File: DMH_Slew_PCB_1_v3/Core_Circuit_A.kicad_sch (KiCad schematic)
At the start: 0 parts

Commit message: V3 sch redesign ongoing
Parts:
- added C10, C11, C3, C4: 100nF, Capacitor_THT:C_Disc_D4.3mm_W1.9mm_P5.00mm, symbol Device:C
- added C14: 22nF, Capacitor_THT:C_Disc_D4.3mm_W1.9mm_P5.00mm, symbol Device:C
- added C15: 220nF, Capacitor_THT:C_Disc_D4.3mm_W1.9mm_P5.00mm, symbol Device:C
- added C6, C7, C8: 10pF, Capacitor_THT:C_Disc_D3.0mm_W2.0mm_P2.50mm, symbol Device:C
- added C9: 2.2nF, Capacitor_THT:C_Disc_D4.3mm_W1.9mm_P5.00mm, symbol Device:C
- added J1, J2, J3: TS_Jack_6.35mm_Sw, SynthStuff:CUI_MJ-63052A, symbol SynthStuff:TS_Jack_6.35mm_Sw
- added J11, J13: Conn_02x03_Top_Bottom, Connector_PinHeader_2.54mm:PinHeader_2x03_P2.54mm_Horizontal, symbol Connector_Generic:Conn_02x03_Top_Bottom
- added J12, J14: Conn_02x06_Top_Bottom, Connector_PinHeader_2.54mm:PinHeader_2x06_P2.54mm_Horizontal, symbol Connector_Generic:Conn_02x06_Top_Bottom
- added J15, J16: Conn_01x08, Connector_PinHeader_2.54mm:PinHeader_1x08_P2.54mm_Vertical, symbol Connector_Generic:Conn_01x08
- added Q1, Q2: BC548, Package_TO_SOT_THT:TO-92L_Inline_Wide, symbol Transistor_BJT:BC548
- added Q3, Q4: BC558, Package_TO_SOT_THT:TO-92L_Inline_Wide, symbol Transistor_BJT:BC558
- added R1, R14, R26: 1k, Resistor_THT:R_Axial_DIN0207_L6.3mm_D2.5mm_P7.62mm_Horizontal, symbol Device:R_US
- added R10, R11, R12, R13, R16, R2, R22, R23, R5, R6, R7, R8, R9: 100k, Resistor_THT:R_Axial_DIN0207_L6.3mm_D2.5mm_P7.62mm_Horizontal, symbol Device:R_US
- added R15, R24, R25: 220k, Resistor_THT:R_Axial_DIN0207_L6.3mm_D2.5mm_P7.62mm_Horizontal, symbol Device:R_US
- added R17: 10k, Resistor_THT:R_Axial_DIN0207_L6.3mm_D2.5mm_P7.62mm_Horizontal, symbol Device:R_US
- added R18, R19, R20, R21: 1k8, Resistor_THT:R_Axial_DIN0207_L6.3mm_D2.5mm_P7.62mm_Horizontal, symbol Device:R_US
- added R3, R4: 56k, Resistor_THT:R_Axial_DIN0207_L6.3mm_D2.5mm_P7.62mm_Horizontal, symbol Device:R_US
- added RV1, RV2: 100k, SynthStuff:Potentiometer_Alpha_RD901F-40-00D_Single_Vertical, symbol Device:R_Potentiometer_US
- added SW1: SW_DPDT_3way, SynthStuff:Toggle_Switch_2_Poles_TE, symbol SynthStuff:Switch_DPDT
- added SW2: SW_DPDT, SynthStuff:Toggle_Switch_2_Poles_TE, symbol SynthStuff:Switch_DPDT
- added SW3: SPDT_OnOffOn, SynthStuff:Toggle_Switch_TE, symbol SynthStuff:SW_SPDT_OnOffOn
- added U1, U2: TL074, Package_DIP:DIP-14_W7.62mm_Socket, symbol Amplifier_Operational:TL074
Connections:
- new net: C8.1, Q1.1 (C), Q4.1 (C), R16.1, U2.13 (-)
- new net: Q4.2 (B), R19.1
- new net: Q1.3 (E), Q2.3 (E), Q3.3 (E), Q4.3 (E), R17.1
- new net: R1.1, R2.1, U1.3 (+)
- new net: C14.1, C15.1, C9.1, Q2.1 (C), Q3.1 (C), U2.6 (-)
- new net: R6.1, R7.1, U2.3 (+)
- new net: C7.2, R15.1, R16.2, U2.8
- new net: R4.2, RV2.3, SW1.2 (B)
- new net: R3.2, RV1.3, SW1.5 (B)
- new net: C8.2, R17.2, U2.14
- new net: R26.2, U2.7
- new net: C7.1, R14.1, U2.9 (-)
- new net: C6.1, R5.1, R8.2, U2.2 (-)
- new net +10V_A: J11.2 (Pin_2), J13.2 (Pin_2), J2.TN, R24.1, R25.1, SW1.1 (A), SW1.6 (C), SW2.4 (A)
- new net +12V: C10.1, C3.1, J11.1 (Pin_1), J13.1 (Pin_1), U1.4 (V+), U2.4 (V+)
- new net -12V: C11.2, C4.2, J11.4 (Pin_4), J13.4 (Pin_4), U1.11 (V-), U2.11 (V-)
- new net A_CV_Buff_C: SW1.3 (C), SW1.4 (A)
- new net A_CV_Buff_M: J14.2 (Pin_2)
- new net A_CV_Buff_S: J12.2 (Pin_2), U1.1, U1.2 (-)
- new net A_CV_In_Jack_M: J14.5 (Pin_5), J2.T
- new net A_CV_In_Jack_S: J12.5 (Pin_5), R1.2
- new net A_Comp_-R: Q2.2 (B), R10.1, R11.1, R18.2
- new net A_Comp_F: Q3.2 (B), R21.1, R23.2, R25.2, R9.1
- new net A_Comp_R: Q1.2 (B), R12.1, R20.2, R22.2, R24.2
- new net A_Diff_Amp_C: SW2.1 (A)
- new net A_Diff_Amp_M: J14.11 (Pin_11)
- new net A_Diff_Amp_S: C6.2, J12.11 (Pin_11), R8.1, U2.1
- new net A_Fall_CV_C: R3.1, RV1.2
- new net A_Fall_CV_M: J14.3 (Pin_3)
- new net A_Fall_CV_S: J12.3 (Pin_3), R23.1
- new net A_Input_Jack_M: J1.T, J14.12 (Pin_12)
- new net A_Input_Jack_S: J12.12 (Pin_12), R13.1, R6.2, U2.10 (+)
- new net A_LinLog_Sw_p2_C: SW2.2 (B)
- new net A_LinLog_Sw_p2_M: J14.7 (Pin_7)
- new net A_LinLog_Sw_p2_S: J12.7 (Pin_7), R10.2, R9.2
- new net A_LinLog_Sw_p5_C: SW2.5 (B)
- new net A_LinLog_Sw_p5_M: J14.8 (Pin_8)
- new net A_LinLog_Sw_p5_S: J12.8 (Pin_8), R11.2, R12.2
- new net A_Out_Jack_C: SW3.2 (B)
- new net A_Out_Jack_M: J14.6 (Pin_6), J3.T
- new net A_Out_Jack_S: C9.2, J12.6 (Pin_6), R14.2, R26.1, R5.2
- new net A_Out_Jack_TN_M: J3.TN
- new net A_Rise_CV_C: R4.1, RV2.2
- new net A_Rise_CV_M: J14.4 (Pin_4)
- new net A_Rise_CV_S: J12.4 (Pin_4), R22.1
- new net A_Rng_Sw_p1_C: SW3.1 (A)
- new net A_Rng_Sw_p1_M: J14.10 (Pin_10)
- new net A_Rng_Sw_p1_S: C14.2, J12.10 (Pin_10)
- new net A_Rng_Sw_p3_C: SW3.3 (C)
- new net A_Rng_Sw_p3_M: J14.9 (Pin_9)
- new net A_Rng_Sw_p3_S: C15.2, J12.9 (Pin_9)
- new net Bus_CV_M: J1.TN
- new net GND: C10.2, C11.1, C3.2, C4.1, J1.S, J11.3 (Pin_3), J11.5 (Pin_5), J11.6 (Pin_6), J13.3 (Pin_3), J13.5 (Pin_5), J13.6 (Pin_6), J2.S, J3.S, R13.2, R15.2, R18.1, R19.2, R2.2, R20.1, R21.2, R7.2, RV1.1, RV2.1, SW2.3 (C), SW2.6 (C), U2.12 (+), U2.5 (+)
- no-connect marks 0 -> 2
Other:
- note added: "22pF in bb"
- note added: "2x SPST switches"

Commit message: Finished PCB1 v3 schematic
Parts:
- added J13, J16: Conn_02x03_Top_Bottom, Connector_PinHeader_2.54mm:PinHeader_2x03_P2.54mm_Horizontal, symbol Connector_Generic:Conn_02x03_Top_Bottom
- added J19, J20: Conn_01x08, Connector_PinHeader_2.54mm:PinHeader_1x08_P2.54mm_Vertical, symbol Connector_Generic:Conn_01x08
- Q1, Q2, Q3, Q4: footprint Package_TO_SOT_THT:TO-92L_Inline_Wide -> Package_TO_SOT_THT:TO-92_Inline
- renumbered J13 to J14, J14 to J15, J15 to J17, J16 to J18
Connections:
- net +10V_A: now also J17.5 (Pin_5), J19.5 (Pin_5)
- net A_CV_Buff_C: now also J19.6 (Pin_6)
- net A_CV_Buff_M: now also J15.4 (Pin_4), J17.6 (Pin_6); no longer J15.2 (Pin_2)
- net A_CV_Buff_S: now also J12.4 (Pin_4); no longer J12.2 (Pin_2)
- net A_CV_In_Jack_M: now also J16.5 (Pin_5); no longer J15.5 (Pin_5)
- net A_CV_In_Jack_S: now also J13.5 (Pin_5); no longer J12.5 (Pin_5)
- net A_Diff_Amp_C: now also J19.2 (Pin_2)
- net A_Diff_Amp_M: now also J15.1 (Pin_1), J17.2 (Pin_2); no longer J15.11 (Pin_11)
- net A_Diff_Amp_S: now also J12.1 (Pin_1); no longer J12.11 (Pin_11)
- net A_Fall_CV_C: now also J19.4 (Pin_4)
- net A_Fall_CV_M: now also J17.4 (Pin_4)
- net A_Input_Jack_M: now also J16.4 (Pin_4); no longer J15.12 (Pin_12)
- net A_Input_Jack_S: now also J13.4 (Pin_4); no longer J12.12 (Pin_12)
- net A_LinLog_Sw_p2_C: now also J20.1 (Pin_1)
- net A_LinLog_Sw_p2_M: now also J18.1 (Pin_1)
- net A_LinLog_Sw_p5_C: now also J20.2 (Pin_2)
- net A_LinLog_Sw_p5_M: now also J18.2 (Pin_2)
- net A_Out_Jack_C: now also J20.6 (Pin_6)
- net A_Out_Jack_M: now also J18.6 (Pin_6), J16.6 (Pin_6); no longer J15.6 (Pin_6)
- net A_Out_Jack_S: now also J13.6 (Pin_6); no longer J12.6 (Pin_6)
- net A_Rise_CV_C: now also J19.3 (Pin_3)
- net A_Rise_CV_M: now also J15.2 (Pin_2), J17.3 (Pin_3); no longer J15.4 (Pin_4)
- net A_Rise_CV_S: now also J12.2 (Pin_2); no longer J12.4 (Pin_4)
- net A_Rng_Sw_p1_C: now also J20.7 (Pin_7)
- net A_Rng_Sw_p1_M: now also J15.12 (Pin_12), J18.7 (Pin_7); no longer J15.10 (Pin_10)
- net A_Rng_Sw_p1_S: now also J12.12 (Pin_12); no longer J12.10 (Pin_10)
- net A_Rng_Sw_p3_C: now also J20.5 (Pin_5)
- net A_Rng_Sw_p3_M: now also J15.11 (Pin_11), J18.5 (Pin_5); no longer J15.9 (Pin_9)
- net A_Rng_Sw_p3_S: now also J12.11 (Pin_11); no longer J12.9 (Pin_9)
- net GND: now also J12.5 (Pin_5), J12.6 (Pin_6), J15.5 (Pin_5), J15.6 (Pin_6), J17.1 (Pin_1), J17.7 (Pin_7), J17.8 (Pin_8), J18.8 (Pin_8), J13.3 (Pin_3), J16.3 (Pin_3), J19.1 (Pin_1), J19.7 (Pin_7), J19.8 (Pin_8), J20.8 (Pin_8)
- net A_F_LED_M: now reaches J18.3 (Pin_3)
- net A_F_LED_M: now also J15.9 (Pin_9)
- net A_R_LED_M: now reaches J18.4 (Pin_4)
- net A_R_LED_M: now also J15.10 (Pin_10)
- new net A_F_Gate_Jack_M: J16.1 (Pin_1)
- new net A_F_Gate_Jack_S: J13.1 (Pin_1)
- new net A_F_LED_C: J20.3 (Pin_3)
- new net A_F_LED_S: J12.9 (Pin_9)
- new net A_R_Gate_Jack_M: J16.2 (Pin_2)
- new net A_R_Gate_Jack_S: J13.2 (Pin_2)
- new net A_R_LED_C: J20.4 (Pin_4)
- new net A_R_LED_S: J12.10 (Pin_10)
- no-connect marks 2 -> 0
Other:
- moved on the sheet: C10, C11, C14, C15, C3, C4, C7, C8, C9, J1, J11, J12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

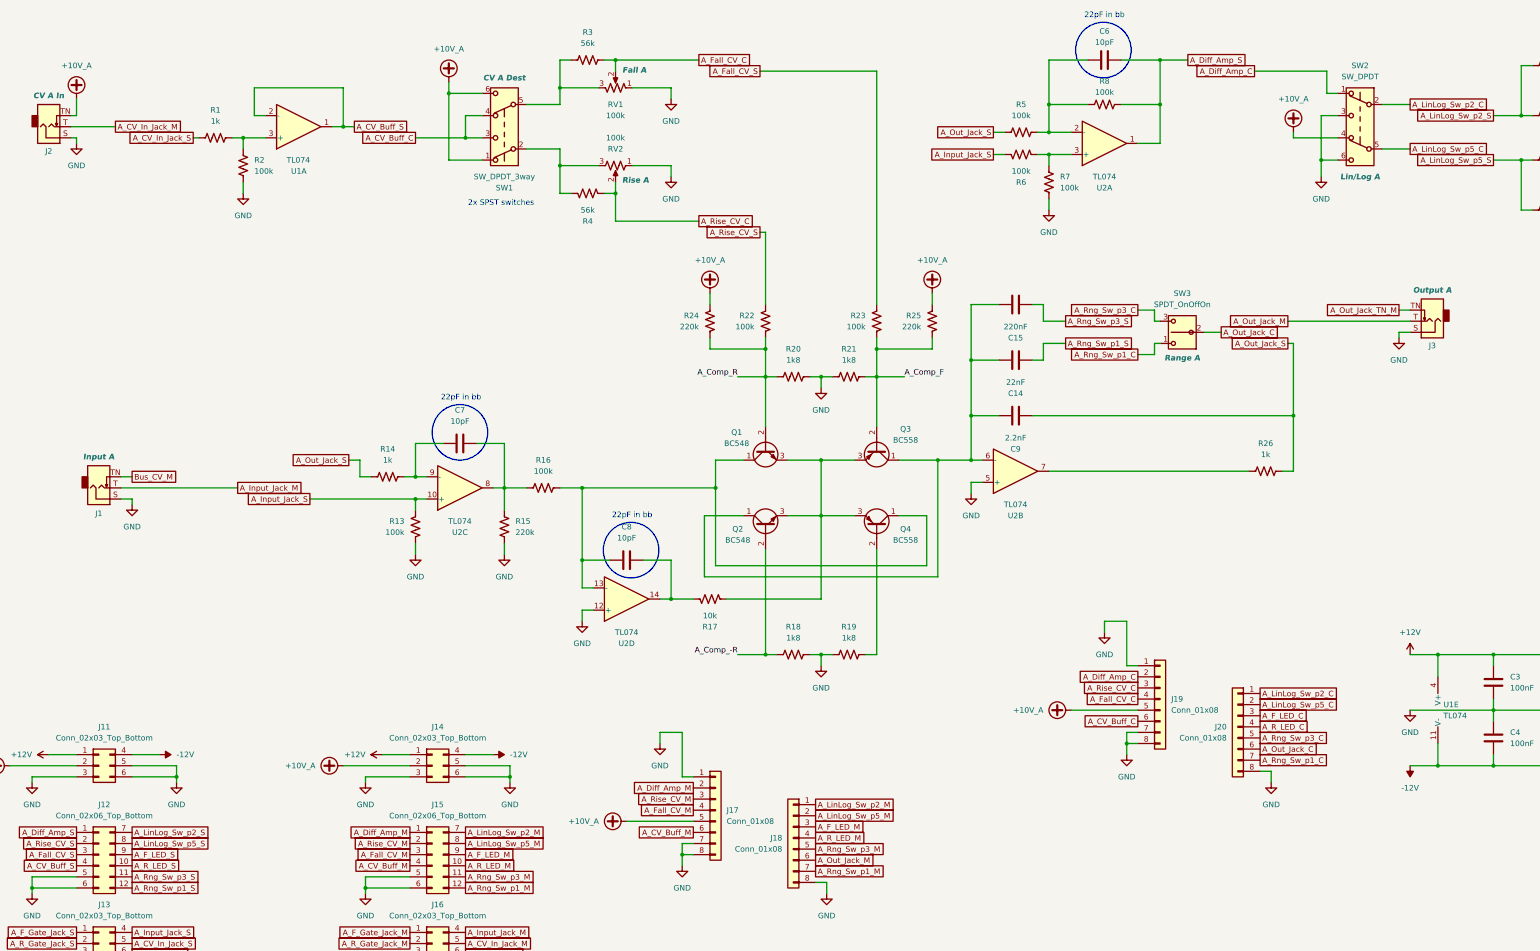
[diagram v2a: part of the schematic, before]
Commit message: Relinked PCB1 and 2 with new v3 schematics
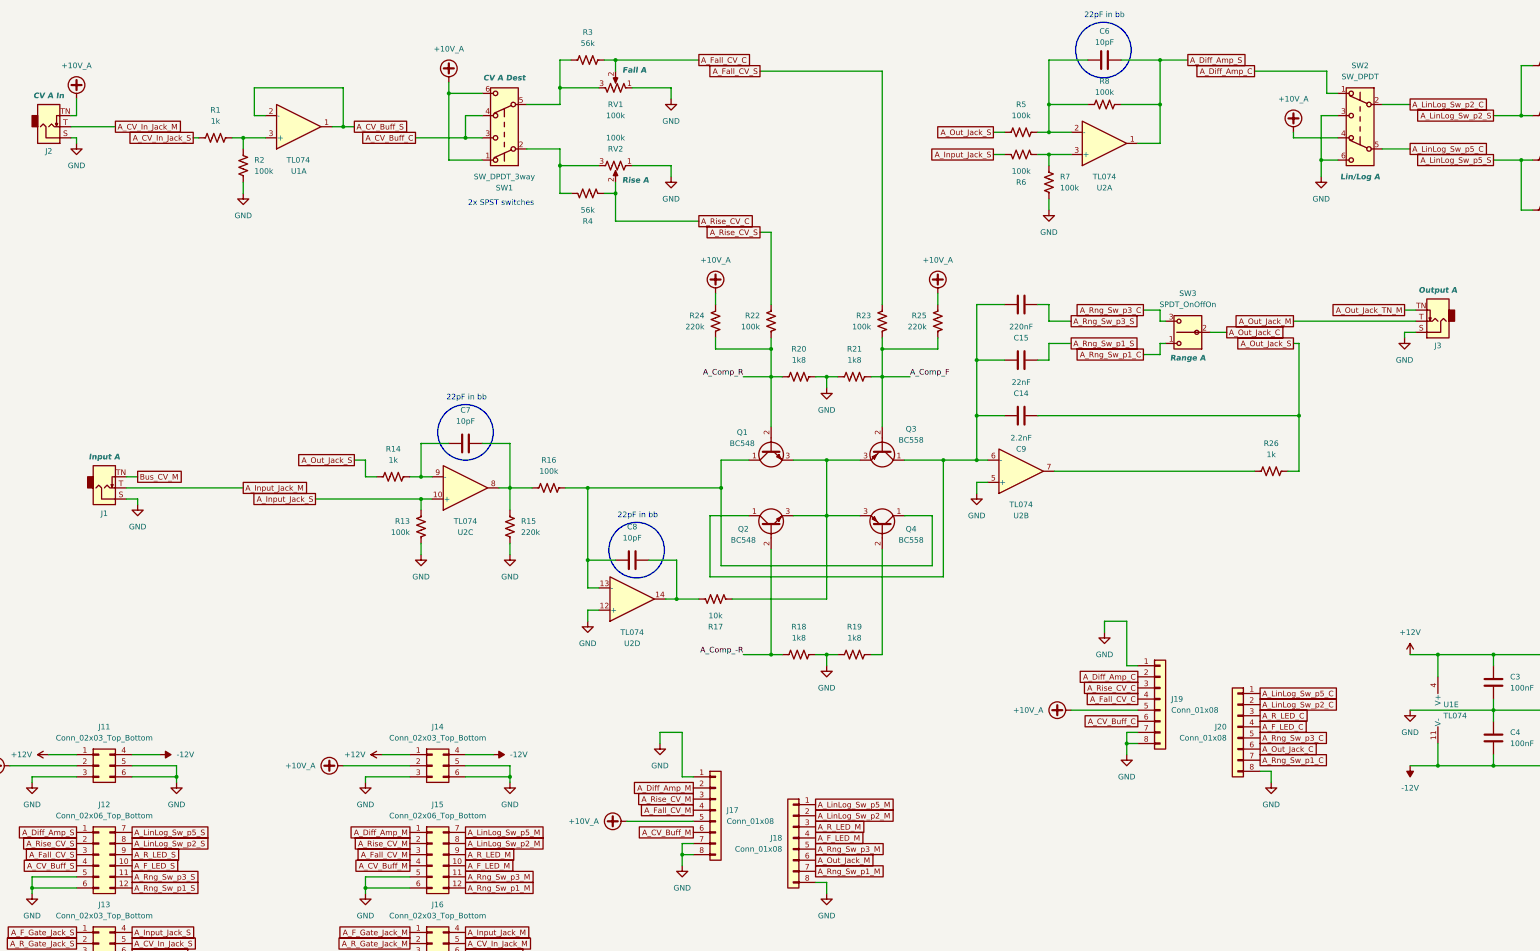
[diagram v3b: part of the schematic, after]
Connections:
- net A_F_LED_C: now also J20.4 (Pin_4); no longer J20.3 (Pin_3)
- net A_F_LED_M: now also J15.10 (Pin_10), J18.4 (Pin_4); no longer J15.9 (Pin_9), J18.3 (Pin_3)
- net A_F_LED_S: now also J12.10 (Pin_10); no longer J12.9 (Pin_9)
- net A_LinLog_Sw_p2_C: now also J20.2 (Pin_2); no longer J20.1 (Pin_1)
- net A_LinLog_Sw_p2_M: now also J15.8 (Pin_8), J18.2 (Pin_2); no longer J15.7 (Pin_7), J18.1 (Pin_1)
- net A_LinLog_Sw_p2_S: now also J12.8 (Pin_8); no longer J12.7 (Pin_7)
- net A_LinLog_Sw_p5_C: now also J20.1 (Pin_1); no longer J20.2 (Pin_2)
- net A_LinLog_Sw_p5_M: now also J15.7 (Pin_7), J18.1 (Pin_1); no longer J15.8 (Pin_8), J18.2 (Pin_2)
- net A_LinLog_Sw_p5_S: now also J12.7 (Pin_7); no longer J12.8 (Pin_8)
- net A_R_LED_C: now also J20.3 (Pin_3); no longer J20.4 (Pin_4)
- net A_R_LED_M: now also J15.9 (Pin_9), J18.3 (Pin_3); no longer J15.10 (Pin_10), J18.4 (Pin_4)
- net A_R_LED_S: now also J12.9 (Pin_9); no longer J12.10 (Pin_10)
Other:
- moved on the sheet: C14, C15, C7, C8, C9, J1, J3, Q1, Q2, Q3, Q4, R13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

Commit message: PCB 1 component placement done
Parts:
- J14, J16: footprint Connector_PinHeader_2.54mm:PinHeader_2x03_P2.54mm_Horizontal -> Connector_PinSocket_2.54mm:PinSocket_2x03_P2.54mm_Vertical
- J15: footprint Connector_PinHeader_2.54mm:PinHeader_2x06_P2.54mm_Horizontal -> Connector_PinSocket_2.54mm:PinSocket_2x06_P2.54mm_Vertical
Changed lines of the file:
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@@
 			)
 		)
-		(property "Footprint" "Connector_PinHeader_2.54mm:PinHeader_2x03_P2.54mm_Horizontal"
+		(property "Footprint" "Connector_PinSocket_2.54mm:PinSocket_2x03_P2.54mm_Vertical"
 			(at 125.73 269.24 0)
 			(effects
@@
 				)
 				(hide yes)
+			)
+		)
+		(property "Function" ""
+			(at 125.73 269.24 0)
+			(effects
+				(font
+					(size 1.27 1.27)
+				)
 			)
 		)
@@
 			)
 		)
-		(property "Footprint" "Connector_PinHeader_2.54mm:PinHeader_2x03_P2.54mm_Horizontal"
+		(property "Footprint" "Connector_PinSocket_2.54mm:PinSocket_2x03_P2.54mm_Vertical"
 			(at 125.73 228.6 0)
 			(effects
@@
 				)
 				(hide yes)
+			)
+		)
+		(property "Function" ""
+			(at 125.73 228.6 0)
+			(effects
+				(font
+					(size 1.27 1.27)
+				)
 			)
 		)
@@
 			)
 		)
-		(property "Footprint" "Connector_PinHeader_2.54mm:PinHeader_2x06_P2.54mm_Horizontal"
+		(property "Footprint" "Connector_PinSocket_2.54mm:PinSocket_2x06_P2.54mm_Vertical"
 			(at 125.73 248.92 0)
 			(effects
@@
 			)
 		)
+		(property "Function" ""
+			(at 125.73 248.92 0)
+			(effects
+				(font
+					(size 1.27 1.27)
+				)
+			)
+		)
